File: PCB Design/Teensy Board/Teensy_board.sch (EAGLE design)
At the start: 5 parts, among them X1 RJ45-8X

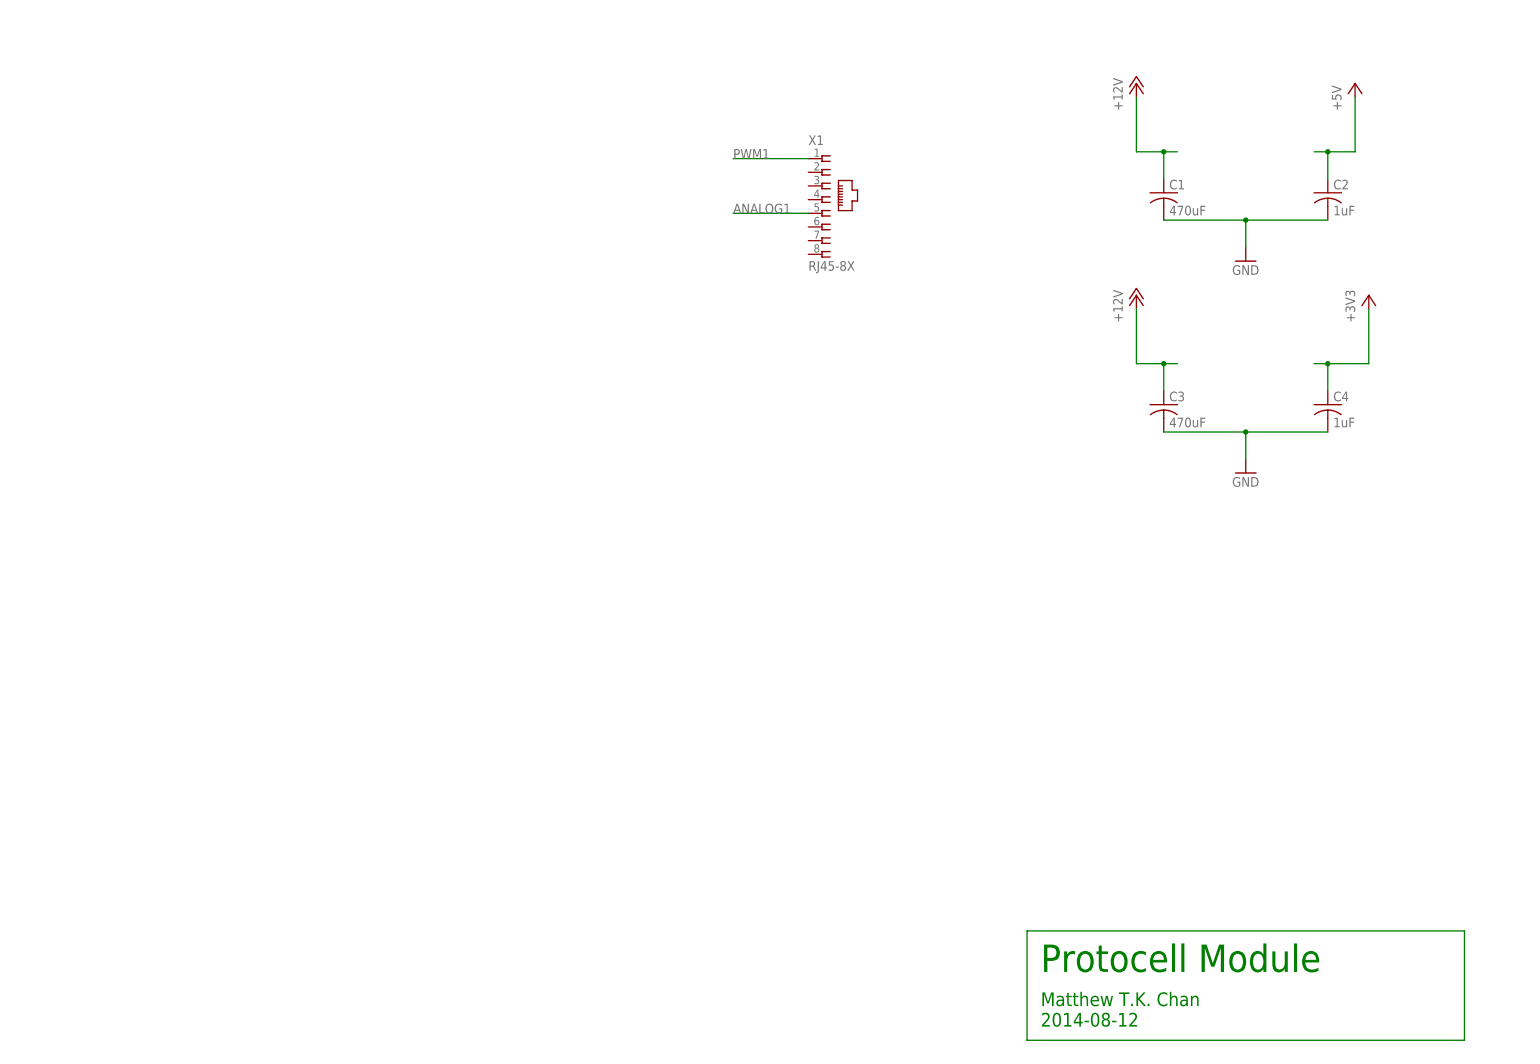
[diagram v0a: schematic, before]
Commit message: Fixed CBLA Lib
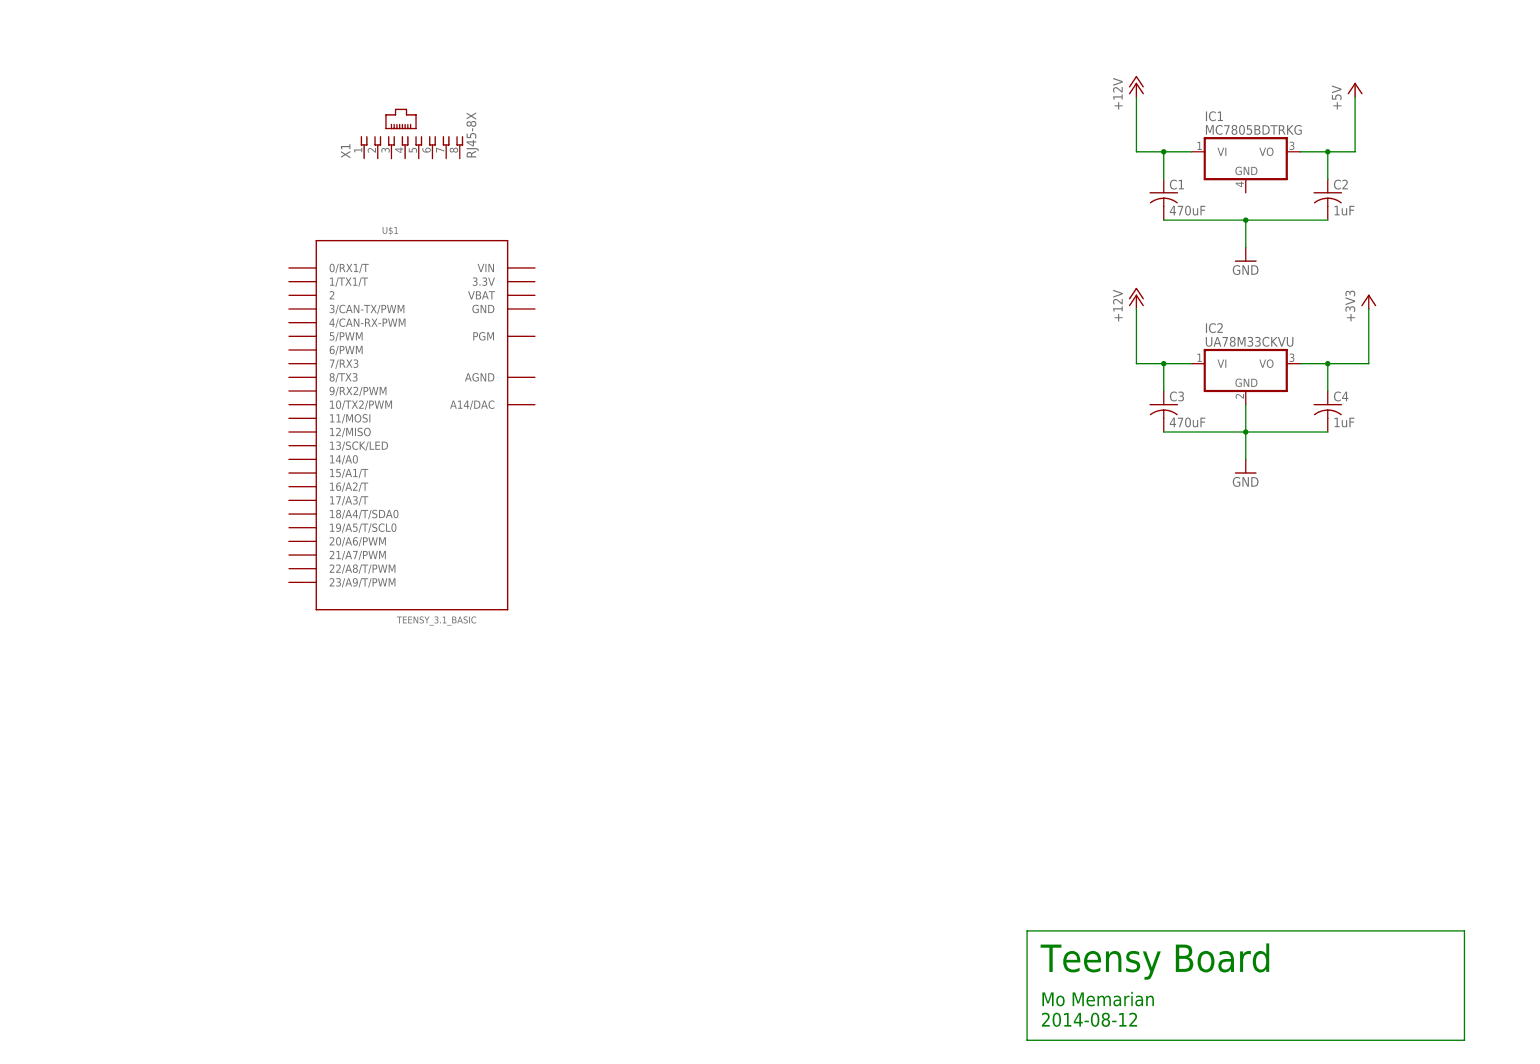
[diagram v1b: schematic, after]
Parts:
- added IC1: MC7805BDTRKG, CBLA_Test_bed_Library:MC7805BDTRKG
- added IC2: UA78M33CKVU, CBLA_Test_bed_Library:UA78M33CKVU
- added U$1: TEENSY_3.1_BASIC, Teensy_3_Series_Board_v1.0:TEENSY_3.1_BASIC
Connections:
- removed net ANALOG1: X1.5
- removed net PWM1: X1.1
- net +12V: now also IC1.VI, IC2.VI
- net +3V3: now also IC2.VO
- net +5V: now also IC1.VO
- net GND: now also IC2.GND
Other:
- note added: "Mo Memarian 2014-08-12"
- note added: "Teensy Board"
- note removed: "Matthew T.K. Chan 2014-08-12"
- note removed: "Protocell Module"
- moved on the sheet: X1
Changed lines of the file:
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@@
 <part name="C4" library="rcl" deviceset="C-US" device="C0603" value="1uF"/>
 <part name="+3V1" library="supply1" deviceset="+3V3" device=""/>
+<part name="IC1" library="CBLA_Test_bed_Library" deviceset="MC78" device="" technology="05BDTRKG"/>
+<part name="IC2" library="CBLA_Test_bed_Library" deviceset="UA78M" device="KVU" technology="33C"/>
+<part name="U$1" library="Teensy_3_Series_Board_v1.0" deviceset="TEENSY_3.1_BASIC" device=""/>
 </parts>
 <sheets>
@@
 <plain>
 <frame x1="0" y1="0" x2="292.1" y2="203.2" columns="8" rows="5" layer="91"/>
-<text x="198.12" y="20.32" size="5.08" layer="91">Protocell Module</text>
-<text x="198.12" y="10.16" size="2.54" layer="91">Matthew T.K. Chan
+<text x="198.12" y="20.32" size="5.08" layer="91">Teensy Board</text>
+<text x="198.12" y="10.16" size="2.54" layer="91">Mo Memarian
 2014-08-12</text>
 </plain>
@@
 <instance part="C1" gate="G$1" x="220.98" y="165.1"/>
 <instance part="C2" gate="G$1" x="251.46" y="165.1"/>
-<instance part="X1" gate="G$1" x="157.48" y="163.83"/>
+<instance part="X1" gate="G$1" x="80.01" y="173.99" rot="R90"/>
 <instance part="P+4" gate="1" x="215.9" y="146.05"/>
 <instance part="GND2" gate="1" x="236.22" y="113.03"/>
@@
 <instance part="C4" gate="G$1" x="251.46" y="125.73"/>
 <instance part="+3V1" gate="G$1" x="259.08" y="146.05"/>
+<instance part="IC1" gate="G$1" x="236.22" y="172.72"/>
+<instance part="IC2" gate="G$1" x="236.22" y="133.35"/>
+<instance part="U$1" gate="G$1" x="81.28" y="123.19"/>
 </instances>
 <busses>
@@
 <wire x1="215.9" y1="172.72" x2="220.98" y2="172.72" width="0.1524" layer="91"/>
 <pinref part="C1" gate="G$1" pin="1"/>
-<wire x1="220.98" y1="172.72" x2="223.52" y2="172.72" width="0.1524" layer="91"/>
 <wire x1="220.98" y1="172.72" x2="220.98" y2="167.64" width="0.1524" layer="91"/>
 <junction x="220.98" y="172.72"/>
+<pinref part="IC1" gate="G$1" pin="VI"/>
+<wire x1="220.98" y1="172.72" x2="226.06" y2="172.72" width="0.1524" layer="91"/>
 </segment>
 <segment>
+<pinref part="IC2" gate="G$1" pin="VI"/>
 <pinref part="P+4" gate="1" pin="+12V"/>
-<wire x1="215.9" y1="143.51" x2="215.9" y2="133.35" width="0.1524" layer="91"/>
-<wire x1="215.9" y1="133.35" x2="220.98" y2="133.35" width="0.1524" layer="91"/>
+<wire x1="226.06" y1="133.35" x2="220.98" y2="133.35" width="0.1524" layer="91"/>
+<wire x1="220.98" y1="133.35" x2="215.9" y2="133.35" width="0.1524" layer="91"/>
+<wire x1="215.9" y1="133.35" x2="215.9" y2="143.51" width="0.1524" layer="91"/>
+<junction x="220.98" y="133.35"/>
 <pinref part="C3" gate="G$1" pin="1"/>
-<wire x1="220.98" y1="133.35" x2="223.52" y2="133.35" width="0.1524" layer="91"/>
-<wire x1="220.98" y1="133.35" x2="220.98" y2="128.27" width="0.1524" layer="91"/>
-<junction x="220.98" y="133.35"/>
+<wire x1="220.98" y1="128.27" x2="220.98" y2="133.35" width="0.1524" layer="91"/>
 </segment>
 </net>
@@
 <segment>
 <pinref part="P+1" gate="1" pin="+5V"/>
-<wire x1="248.92" y1="172.72" x2="251.46" y2="172.72" width="0.1524" layer="91"/>
 <wire x1="251.46" y1="172.72" x2="256.54" y2="172.72" width="0.1524" layer="91"/>
 <wire x1="256.54" y1="172.72" x2="256.54" y2="182.88" width="0.1524" layer="91"/>
@@
 <wire x1="251.46" y1="172.72" x2="251.46" y2="167.64" width="0.1524" layer="91"/>
 <junction x="251.46" y="172.72"/>
+<pinref part="IC1" gate="G$1" pin="VO"/>
+<wire x1="251.46" y1="172.72" x2="246.38" y2="172.72" width="0.1524" layer="91"/>
 </segment>
 </net>
@@
 <pinref part="C4" gate="G$1" pin="2"/>
 <wire x1="236.22" y1="120.65" x2="251.46" y2="120.65" width="0.1524" layer="91"/>
-</segment>
-</net>
-<net name="PWM1" class="0">
-<segment>
-<pinref part="X1" gate="G$1" pin="1"/>
-<wire x1="154.94" y1="171.45" x2="140.97" y2="171.45" width="0.1524" layer="91"/>
-<label x="140.97" y="171.45" size="1.778" layer="95"/>
-</segment>
-</net>
-<net name="ANALOG1" class="0">
-<segment>
-<pinref part="X1" gate="G$1" pin="5"/>
-<wire x1="154.94" y1="161.29" x2="140.97" y2="161.29" width="0.1524" layer="91"/>
-<label x="140.97" y="161.29" size="1.778" layer="95"/>
+<pinref part="IC2" gate="G$1" pin="GND"/>
+<wire x1="236.22" y1="125.73" x2="236.22" y2="120.65" width="0.1524" layer="91"/>
 </segment>
 </net>
@@
 <wire x1="259.08" y1="133.35" x2="251.46" y2="133.35" width="0.1524" layer="91"/>
 <junction x="251.46" y="133.35"/>
-<wire x1="251.46" y1="133.35" x2="248.92" y2="133.35" width="0.1524" layer="91"/>
 <pinref part="C4" gate="G$1" pin="1"/>
 <wire x1="251.46" y1="133.35" x2="251.46" y2="128.27" width="0.1524" layer="91"/>
+<pinref part="IC2" gate="G$1" pin="VO"/>
+<wire x1="251.46" y1="133.35" x2="246.38" y2="133.35" width="0.1524" layer="91"/>
 </segment>
 </net>

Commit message: Teensy Board change
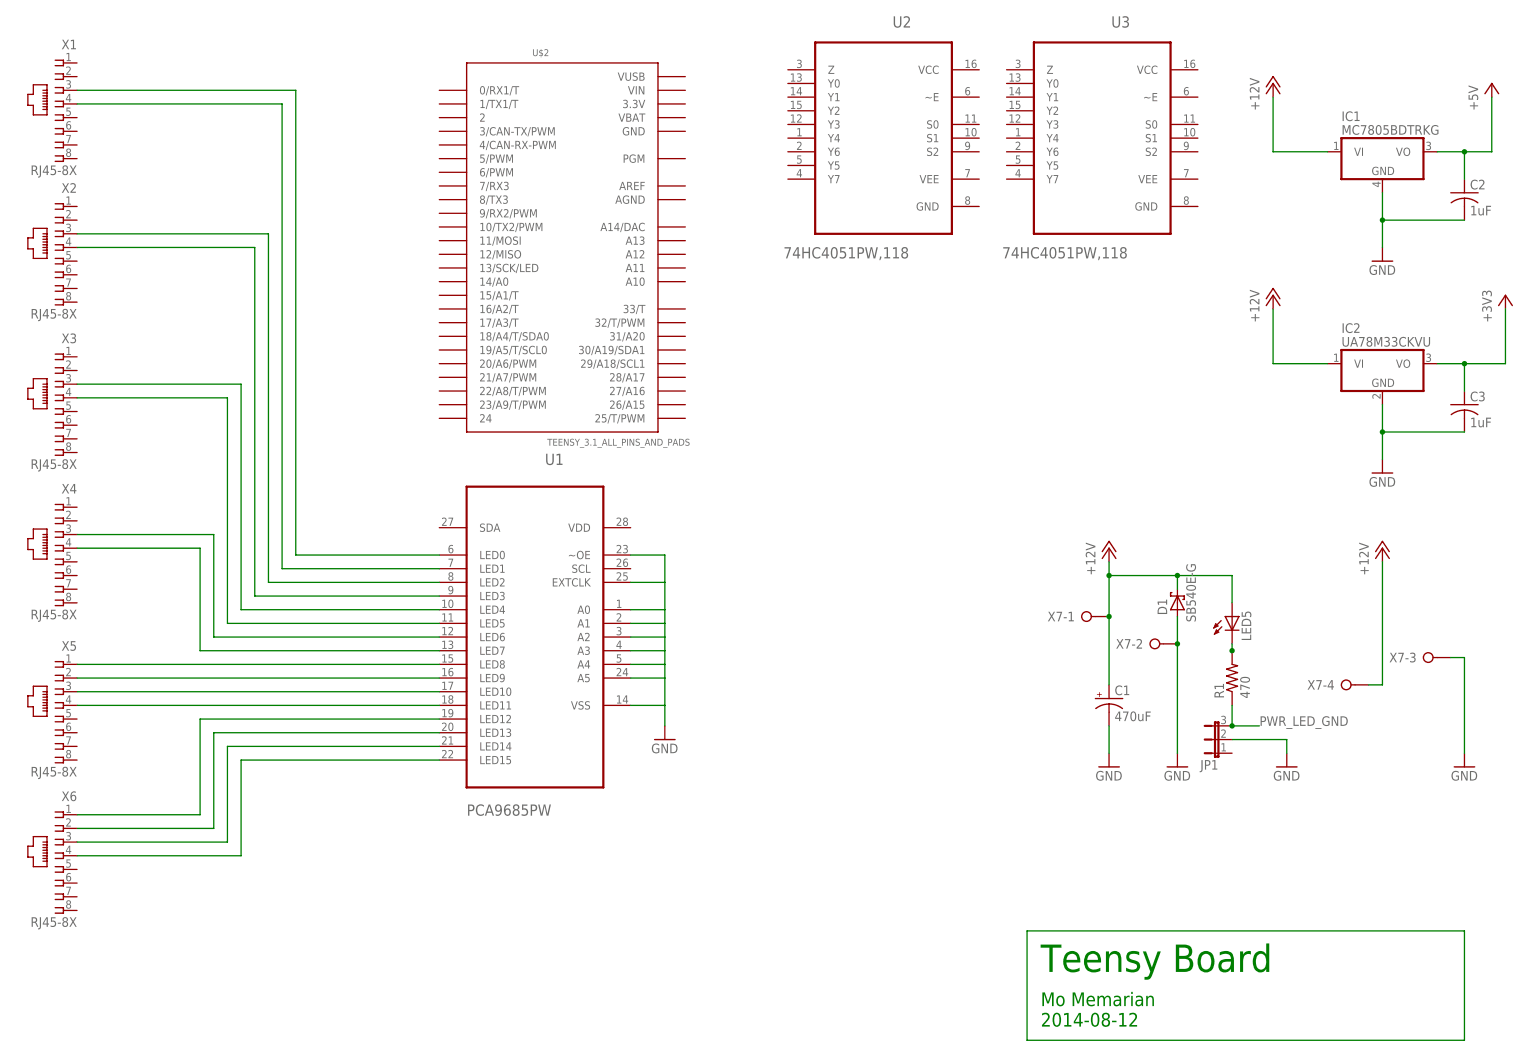
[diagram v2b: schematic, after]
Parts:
- removed C4: 1uF, rcl:C-USC0603
- removed U$1: TEENSY_3.1_BASIC, Teensy_3_Series_Board_v1.0:TEENSY_3.1_BASIC
- added D1: SB540E-G, CBLA_Test_bed_Library:SB540E-G
- added JP1: (no value), jumper:JP2E
- added LED5: (no value), led:LEDSML1206
- added R1: 470, CBLA_Test_bed_Library:R-US_R0603
- added U$2: TEENSY_3.1_ALL_PINS_AND_PADS, Teensy_3_Series_Board_v1.0:TEENSY_3.1_ALL_PINS_AND_PADS
- added U1: PCA9685PW, NXP_By_element14_Batch_1:PCA9685PW
- added U2, U3: 74HC4051PW,118, NXP_By_element14_Batch_1:74HC4051PW,118
- added X2, X3, X4, X5, X6: RJ45-8X, CBLA_Test_bed_Library:RJ45-8X
- added X7: (no value), con-wago-508:W237-04P
- C1: device rcl:C-USC0603 -> rcl:CPOL-USE5-10.5
- C3: value 470uF -> 1uF
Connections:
- new net N$1: U1.LED0, X1.3
- new net N$10: LED5.C, R1.2
- new net N$11: U1.LED8, X5.1
- new net N$12: U1.LED9, X5.2
- new net N$13: U1.LED10, X5.3
- new net N$14: U1.LED11, X5.4
- new net N$15: U1.LED12, X6.1
- new net N$16: U1.LED13, X6.2
- new net N$17: U1.LED14, X6.3
- new net N$18: U1.LED15, X6.4
- new net N$2: U1.LED1, X1.4
- new net N$3: U1.LED2, X2.3
- new net N$4: U1.LED3, X2.4
- new net N$5: U1.LED4, X3.3
- new net N$6: U1.LED5, X3.4
- new net N$7: U1.LED6, X4.3
- new net N$8: U1.LED7, X4.4
- new net PWR_LED_GND: JP1.3, R1.1
- net +12V: now also C1.+, D1.C, LED5.A, X7-1.KL, X7-4.KL; no longer C1.1, C3.1
- net +3V3: now also C3.1; no longer C4.1
- net GND: now also C1.-, D1.A, IC1.GND, JP1.2, U1.A0, U1.A1, U1.A2, U1.A3, U1.A4, U1.A5, U1.EXTCLK, U1.VSS, U1.~OE, X7-2.KL, X7-3.KL; no longer C1.2, C4.2
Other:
- moved on the sheet: C2, C3, IC1, IC2, X1

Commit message: Teensy Board Update
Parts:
- added C4, C5: 100nF, rcl:C-USC0603
- added LED2, LED3: (no value), led:LEDSML1206
- added R2, R3: 4k7, CBLA_Test_bed_Library:R-US_R0603
- added R4, R5: 470, CBLA_Test_bed_Library:R-US_R0603
- renumbered LED5 to LED1
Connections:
- new net FPWM_1_1: U$2.3/CAN-TX/PWM, X1.1
- new net FPWM_1_2: U$2.4/CAN-RX-PWM, X1.2
- new net FPWM_2_1: U$2.5/PWM, X2.1
- new net FPWM_2_2: U$2.6/PWM, X2.2
- new net FPWM_3_1: U$2.22/A8/T/PWM, X3.1
- new net FPWM_3_2: U$2.23/A9/T/PWM, X3.2
- new net FPWM_4_1: U$2.25/T/PWM, X4.1
- new net FPWM_4_2: U$2.32/T/PWM, X4.2
- new net MUL_ADR_0: U$2.2, U2.S0, U3.S0
- new net MUL_ADR_1: U$2.24, U2.S1, U3.S1
- new net MUL_ADR_2: U$2.33/T, U2.S2, U3.S2
- new net MUL_SCL: U$2.19/A5/T/SCL0, U3.Z
- new net MUL_SCL_1: U3.Y0, X1.7
- new net MUL_SCL_2: U3.Y1, X2.7
- new net MUL_SCL_3: U3.Y2, X3.7
- new net MUL_SCL_4: U3.Y3, X4.7
- new net MUL_SCL_5: U3.Y4, X5.7
- new net MUL_SCL_6: U3.Y5, X6.7
- new net MUL_SDA: U$2.18/A4/T/SDA0, U2.Z
- new net MUL_SDA_1: U2.Y0, X1.8
- new net MUL_SDA_2: U2.Y1, X2.8
- new net MUL_SDA_3: U2.Y2, X3.8
- new net MUL_SDA_4: U2.Y3, X4.8
- new net MUL_SDA_5: U2.Y4, X5.8
- new net MUL_SDA_6: U2.Y5, X6.8
- new net N$19: LED3.C, R5.2
- new net N$31: X1.5
- new net N$32: X1.6
- new net N$33: U1.LED15
- new net N$35: X2.5
- new net N$36: X2.6
- new net N$39: X3.5
- new net N$40: X3.6
- new net N$43: X4.5
- new net N$44: X4.6
- new net N$47: X5.5
- new net N$48: X5.6
- new net N$51: X6.5
- new net N$52: X6.6
- new net SCL_PWM: R3.1, U$2.29/A18/SCL1, U1.SCL
- new net SDA_PWM: R2.1, U$2.30/A19/SDA1, U1.SDA
- net +3V3: now also C5.1, LED2.A, R2.2, R3.2, U1.VDD
- net +5V: now also C4.1, LED3.A
- net GND: now also C4.2, C5.2, R4.1, R5.1
- net N$18: now also LED2.C, R4.2; no longer U1.LED15, X6.4
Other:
- moved on the sheet: C2, C3, IC1, IC2, U2, U3

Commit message: Teensy Board
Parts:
- added JP2, JP3: (no value), jumper:JP2E
- added R6: 4k7, CBLA_Test_bed_Library:R-US_R0603
- added T1: (no value), CBLA_Test_bed_Library:NTD5867NLT4G
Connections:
- removed net N$31: X1.5
- removed net N$32: X1.6
- removed net N$35: X2.5
- removed net N$36: X2.6
- removed net N$39: X3.5
- removed net N$40: X3.6
- removed net N$43: X4.5
- removed net N$44: X4.6
- removed net N$47: X5.5
- removed net N$48: X5.6
- removed net N$51: X6.5
- removed net N$52: X6.6
- new net 3V3INT: JP3.2, R2.2, R3.2, U1.VDD, U2.VCC, U3.VCC
- new net A0: U$2.14/A0, X1.5
- new net A1: U$2.15/A1/T, X1.6
- new net A12: U$2.A12, X3.5
- new net A13: U$2.A13, X3.6
- new net A15: U$2.26/A15, X4.5
- new net A16: U$2.27/A16, X5.5
- new net A17: U$2.28/A17, X5.6
- new net A2: U$2.16/A2/T, X2.5
- new net A20: U$2.31/A20, X4.6
- new net A3: U$2.17/A3/T, X2.6
- new net A6: U$2.20/A6/PWM, X6.5
- new net A7: U$2.21/A7/PWM, X6.6
- new net N$20: R6.2, T1.G
- new net PGM: T1.D, U$2.PGM
- new net TEENSY_3V3: JP3.3, U$2.3.3V
- new net TEENSY_VIN: JP2.2, U$2.VIN
- net +3V3: now also JP3.1; no longer R2.2, R3.2, U1.VDD
- net +5V: now also JP2.1
- net GND: now also R6.1, T1.S, U$2.GND, U2.GND, U2.VEE, U2.~E, U3.GND, U3.VEE, U3.~E
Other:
- moved on the sheet: C2, C3, C4, C5, IC1, IC2, LED2, LED3, R4, R5, U2, U3
